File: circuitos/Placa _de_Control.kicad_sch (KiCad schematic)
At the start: 24 parts, among them J1 Screw_Terminal_01x02, J2 Screw_Terminal_01x02, J3 Screw_Terminal_01x02, J4 Screw_Terminal_01x16, J5 Screw_Terminal_01x03, Q1 BC337, U1 LM1117-3.3

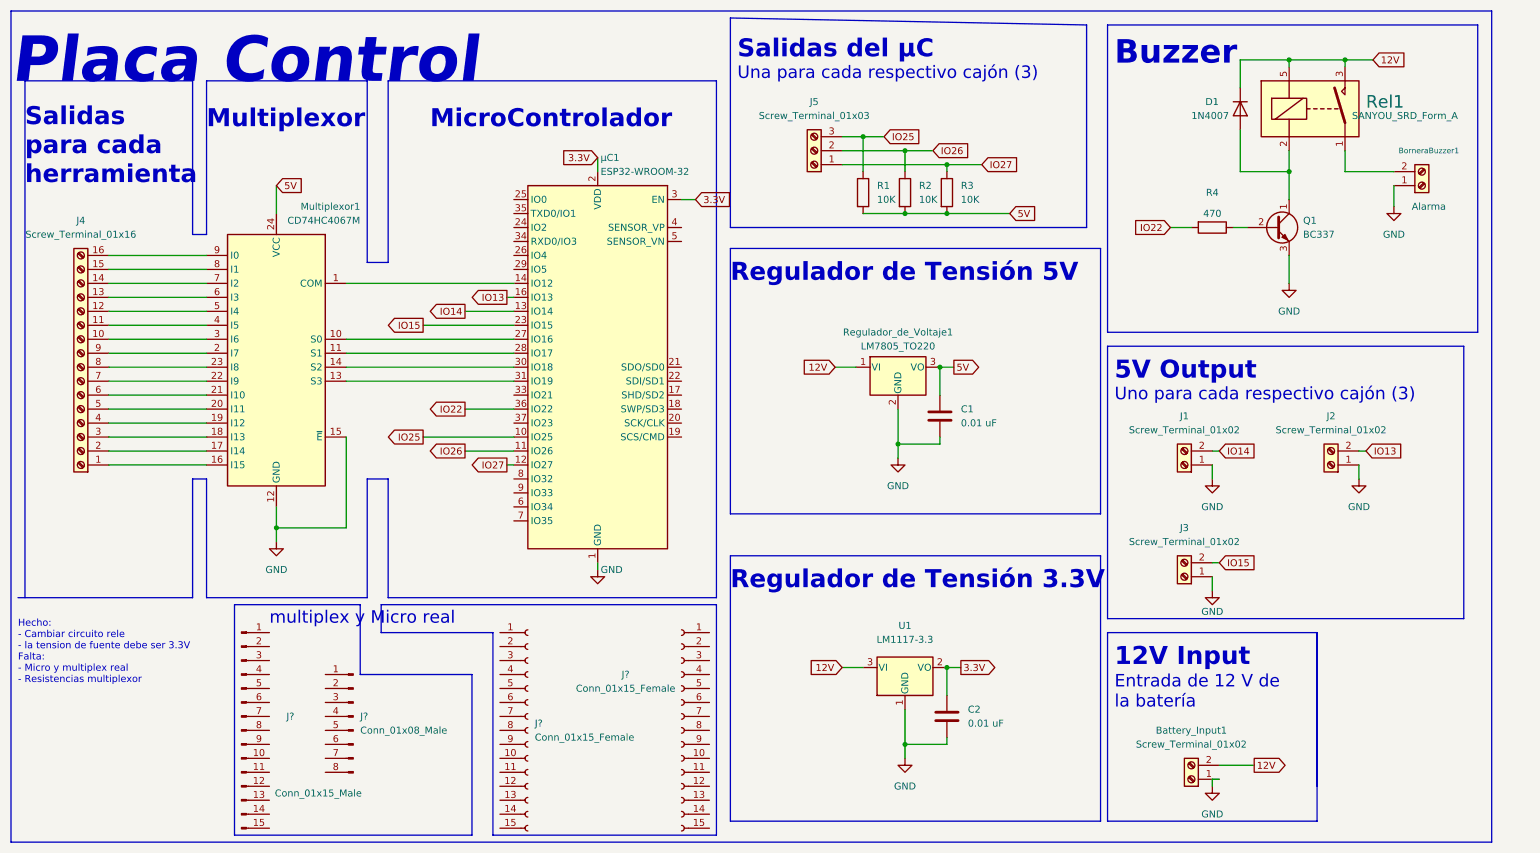
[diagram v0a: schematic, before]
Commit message: feat: actualizar esquematico placa de control (#63)
* refactor: borrar esquematico descontinuado

* feat: agregar esquematico actualizado
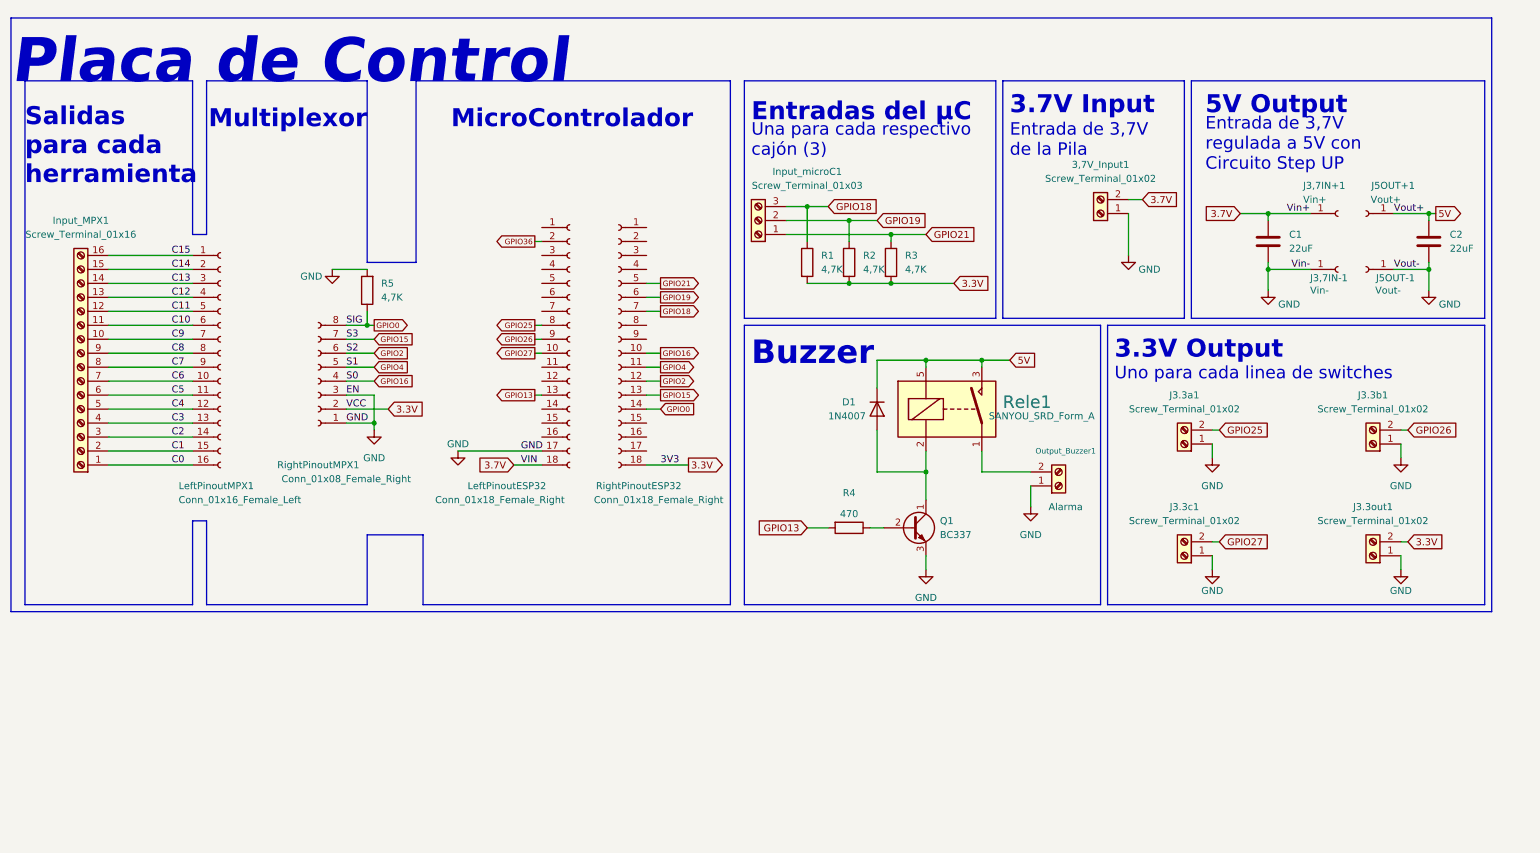
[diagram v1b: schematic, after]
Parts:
- removed J? (x2): Conn_01x15_Female, symbol Connector:Conn_01x15_Female
- removed J?: Conn_01x15_Male, symbol Connector:Conn_01x15_Male
- removed J?: Conn_01x08_Male, symbol Connector:Conn_01x08_Male
- removed Multiplexor1: CD74HC4067M, Package_SO:SOIC-24W_7.5x15.4mm_P1.27mm, symbol 74xx:CD74HC4067M
- removed Regulador_de_Voltaje1: LM7805_TO220, Package_TO_SOT_THT:TO-220-3_Vertical, symbol Regulator_Linear:LM7805_TO220
- removed U1: LM1117-3.3, symbol Regulator_Linear:LM1117-3.3
- removed µC1: ESP32-WROOM-32, RF_Module:ESP32-WROOM-32, symbol RF_Module:ESP32-WROOM-32
- added J3,7IN+1: Vin+, Connector_PinSocket_2.54mm:PinSocket_1x01_P2.54mm_Vertical, symbol Connector:Conn_01x01_Female
- added J3,7IN-1: Vin-, Connector_PinSocket_2.54mm:PinSocket_1x01_P2.54mm_Vertical, symbol Connector:Conn_01x01_Female
- added J3.3out1: Screw_Terminal_01x02, TerminalBlock:TerminalBlock_bornier-2_P5.08mm, symbol Connector:Screw_Terminal_01x02
- added J5OUT+1: Vout+, Connector_PinSocket_2.54mm:PinSocket_1x01_P2.54mm_Vertical, symbol Connector:Conn_01x01_Female
- added J5OUT-1: Vout-, Connector_PinSocket_2.54mm:PinSocket_1x01_P2.54mm_Vertical, symbol Connector:Conn_01x01_Female
- added LeftPinoutESP32: Conn_01x18_Female_Right, Connector_PinHeader_2.54mm:PinHeader_1x18_P2.54mm_Vertical, symbol Connector:Conn_01x18_Female
- added LeftPinoutMPX1: Conn_01x16_Female_Left, Connector_PinSocket_2.54mm:PinSocket_1x16_P2.54mm_Vertical, symbol Connector:Conn_01x16_Female
- added R5: 4,7K, Resistor_THT:R_Axial_DIN0204_L3.6mm_D1.6mm_P1.90mm_Vertical, symbol Device:R
- added RightPinoutESP32: Conn_01x18_Female_Right, Connector_PinSocket_2.54mm:PinSocket_1x18_P2.54mm_Vertical, symbol Connector:Conn_01x18_Female
- added RightPinoutMPX1: Conn_01x08_Female_Right, Connector_PinSocket_2.54mm:PinSocket_1x08_P2.54mm_Vertical, symbol Connector:Conn_01x08_Female
- C1, C2: value 0.01 uF -> 22uF; footprint Capacitor_SMD:CP_Elec_3x5.3 -> Capacitor_THT:C_Axial_L3.8mm_D2.6mm_P7.50mm_Horizontal
- R1, R2, R3: value 10K -> 4,7K; footprint Resistor_SMD:R_0201_0603Metric -> Resistor_THT:R_Axial_DIN0204_L3.6mm_D1.6mm_P1.90mm_Vertical
- R4: footprint Resistor_SMD:R_0201_0603Metric -> Resistor_THT:R_Axial_DIN0204_L3.6mm_D1.6mm_P1.90mm_Vertical
- renumbered Battery_Input1 to 3,7V_Input1, J4 to Input_MPX1, J5 to Input_microC1, J1 to J3.3a1, J2 to J3.3b1, J3 to J3.3c1, BorneraBuzzer1 to Output_Buzzer1, Rel1 to Rele1
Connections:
- net 3.3V: now also R1.2, R2.2, R3.2, J3.3out1.2 (Pin_2), RightPinoutESP32.18 (Pin_18), RightPinoutMPX1.2 (Pin_2); no longer C2.1
- net 5V: now also C2.1, D1.1 (K), Rele1.3, Rele1.5, J5OUT+1.1 (Pin_1); no longer C1.1, R1.2, R2.2, R3.2
- net GND: now also J3,7IN-1.1 (Pin_1), J3.3out1.1 (Pin_1), J5OUT-1.1 (Pin_1), LeftPinoutESP32.17 (Pin_17), R5.2, RightPinoutMPX1.1 (Pin_1), RightPinoutMPX1.3 (Pin_3)
- net C0: now reaches Input_MPX1.1 (Pin_1)
- net C0: now also LeftPinoutMPX1.16 (Pin_16)
- net C1: now reaches Input_MPX1.2 (Pin_2)
- net C1: now also LeftPinoutMPX1.15 (Pin_15)
- net C2: now reaches Input_MPX1.3 (Pin_3)
- net C2: now also LeftPinoutMPX1.14 (Pin_14)
- net C3: now reaches Input_MPX1.4 (Pin_4)
- net C3: now also LeftPinoutMPX1.13 (Pin_13)
- net C8: now reaches Input_MPX1.9 (Pin_9)
- net C8: now also LeftPinoutMPX1.8 (Pin_8)
- net C4: now reaches Input_MPX1.5 (Pin_5)
- net C4: now also LeftPinoutMPX1.12 (Pin_12)
- net C5: now reaches Input_MPX1.6 (Pin_6)
- net C5: now also LeftPinoutMPX1.11 (Pin_11)
- net C6: now reaches Input_MPX1.7 (Pin_7)
- net C6: now also LeftPinoutMPX1.10 (Pin_10)
- net C7: now reaches Input_MPX1.8 (Pin_8)
- net C7: now also LeftPinoutMPX1.9 (Pin_9)
- net C9: now reaches Input_MPX1.10 (Pin_10)
- net C9: now also LeftPinoutMPX1.7 (Pin_7)
- net C10: now reaches Input_MPX1.11 (Pin_11)
- net C10: now also LeftPinoutMPX1.6 (Pin_6)
- net C11: now reaches Input_MPX1.12 (Pin_12)
- net C11: now also LeftPinoutMPX1.5 (Pin_5)
- net C12: now reaches Input_MPX1.13 (Pin_13)
- net C12: now also LeftPinoutMPX1.4 (Pin_4)
- net C13: now reaches Input_MPX1.14 (Pin_14)
- net C13: now also LeftPinoutMPX1.3 (Pin_3)
- net C14: now reaches Input_MPX1.15 (Pin_15)
- net C14: now also LeftPinoutMPX1.2 (Pin_2)
- net C15: now reaches Input_MPX1.16 (Pin_16)
- net C15: now also LeftPinoutMPX1.1 (Pin_1)
- removed net 12V: 3,7V_Input1.2 (Pin_2), D1.1 (K), Rele1.3, Rele1.5
- net IO13 renamed GPIO26
- net GPIO26: now also LeftPinoutESP32.9 (Pin_9)
- net IO14 renamed GPIO25
- net GPIO25: now also LeftPinoutESP32.8 (Pin_8)
- net IO15 renamed GPIO27
- net GPIO27: now also LeftPinoutESP32.10 (Pin_10)
- net IO22 renamed GPIO13
- net GPIO13: now also LeftPinoutESP32.13 (Pin_13)
- net IO25 renamed GPIO18
- net GPIO18: now also RightPinoutESP32.7 (Pin_7)
- net IO26 renamed GPIO19
- net GPIO19: now also RightPinoutESP32.6 (Pin_6)
- net IO27 renamed GPIO21
- net GPIO21: now also RightPinoutESP32.5 (Pin_5)
- new net 3.7V: 3,7V_Input1.2 (Pin_2), C1.1, J3,7IN+1.1 (Pin_1), LeftPinoutESP32.18 (Pin_18)
- new net GPIO0: R5.1, RightPinoutESP32.14 (Pin_14), RightPinoutMPX1.8 (Pin_8)
- new net GPIO15: RightPinoutESP32.13 (Pin_13), RightPinoutMPX1.7 (Pin_7)
- new net GPIO16: RightPinoutESP32.10 (Pin_10), RightPinoutMPX1.4 (Pin_4)
- new net GPIO2: RightPinoutESP32.12 (Pin_12), RightPinoutMPX1.6 (Pin_6)
- new net GPIO36: LeftPinoutESP32.2 (Pin_2)
- new net GPIO4: RightPinoutESP32.11 (Pin_11), RightPinoutMPX1.5 (Pin_5)
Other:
- note added: "3.3V Output"
- note added: "3.7V Input"
- note added: "Entrada de 3,7V de la Pila"
- note added: "Entrada de 3,7V regulada a 5V con Circuito Step UP"
- note added: "Entradas del μC"
- note added: "Placa de Control"
- note added: "Uno para cada linea de switches"
- note removed: "12V Input"
- note removed: "Entrada de 12 V de la batería"
- note removed: "Hecho: - Cambiar circuito rele - la tension de fuente debe ser 3.3V Falta: - Micro y multiplex real - Resistencias multiplexor"
- note removed: "Placa Control"
- note removed: "Regulador de Tensión 3.3V"
- note removed: "Regulador de Tensión 5V"
- note removed: "Salidas del μC"
- note removed: "Uno para cada respectivo cajón (3)"
- note removed: "multiplex y Micro real"
- moved on the sheet: 3,7V_Input1, D1, Input_microC1, J3.3a1, J3.3b1, J3.3c1, Output_Buzzer1, Q1, R1, R2, R3, R4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
